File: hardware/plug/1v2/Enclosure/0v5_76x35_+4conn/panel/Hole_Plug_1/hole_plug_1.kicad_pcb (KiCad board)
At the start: 2 copper layers, 13.9 x 3.8 mm, 3 parts

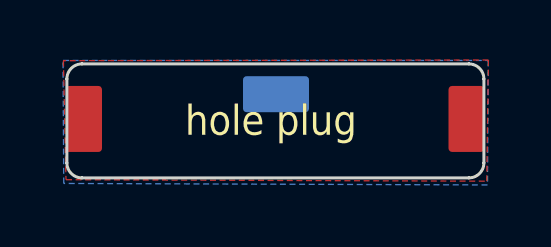
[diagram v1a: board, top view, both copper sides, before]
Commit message: add 3d models in .wrl
used @2ftg .step models and imported them into FreeCAD
added .wrl for Rear panels and hole plugs
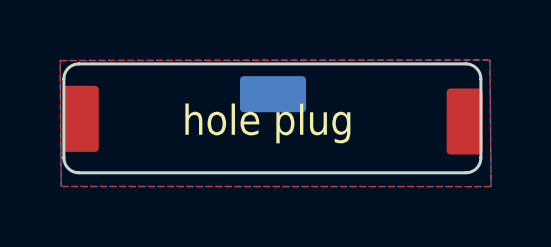
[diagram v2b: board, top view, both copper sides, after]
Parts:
- moved REF** 0.11 mm to (57.1, 117.4)
- moved REF** 0.10 mm to (69.9, 117.5)
- moved REF** 0.10 mm to (63.5, 116.6)
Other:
- board size 13.9 x 3.8 mm -> 13.9 x 3.6 mm
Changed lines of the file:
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@@
     (links 2)
     (no_connects 1)
-    (area 52.800953 112.2525 74.339048 124.249079)
+    (area 56.474999 115.499999 70.475001 119.230001)
     (thickness 1.6)
     (drawings 29)
@@
     (pad_to_mask_clearance 0)
     (aux_axis_origin 56.42 115.36)
-    (grid_origin 56.42 115.36)
+    (grid_origin 57.125 115.55)
     (visible_elements 7FFFFFFF)
     (pcbplotparams
@@
   )
   (module Connect:1pin (layer B.Cu)
-    (at 63.595 116.56 270)
+    (at 63.495 116.56 270)
     (descr "module 1 pin (ou trou mecanique de percage)")
     (tags DEV)
@@
   )
   (module Connect:1pin (layer F.Cu)
-    (at 57.195 117.385)
+    (at 57.085 117.38)
     (descr "module 1 pin (ou trou mecanique de percage)")
     (tags DEV)
@@
   )
   (module Connect:1pin (layer F.Cu)
-    (at 69.945 117.385)
+    (at 69.885 117.47)
     (descr "module 1 pin (ou trou mecanique de percage)")
     (tags DEV)
@@
       (net 1 GND) (zone_connect 1) (thermal_width 0.5) (thermal_gap 0.3))
   )
-  (gr_text "hole plug" (at 63.425 117.45) (layer F.SilkS)
+  (gr_text "hole plug" (at 63.325 117.45) (layer F.SilkS)
     (effects (font (size 1 0.9) (thickness 0.2)))
   )
-  (gr_line (start 57.125 119.35) (end 70.025 119.35) (layer Edge.Cuts) (width 0.1))
-  (gr_line (start 56.625 116.05) (end 56.625 118.85) (layer Edge.Cuts) (width 0.1))
-  (gr_line (start 70.025 115.55) (end 57.125 115.55) (layer Edge.Cuts) (width 0.1))
-  (gr_line (start 70.525 118.85) (end 70.525 116.05) (layer Edge.Cuts) (width 0.1))
-  (gr_arc (start 70.025 118.85) (end 70.525 118.85) (angle 90) (layer Edge.Cuts) (width 0.1))
-  (gr_arc (start 70.025 116.05) (end 70.025 115.55) (angle 90) (layer Edge.Cuts) (width 0.1))
-  (gr_arc (start 57.125 116.05) (end 56.625 116.05) (angle 90) (layer Edge.Cuts) (width 0.1))
-  (gr_arc (start 57.125 118.85) (end 57.125 119.35) (angle 90) (layer Edge.Cuts) (width 0.1))
+  (gr_line (start 57.025 119.18) (end 69.925 119.18) (layer Edge.Cuts) (width 0.1))
+  (gr_line (start 56.525 116.05) (end 56.525 118.68) (layer Edge.Cuts) (width 0.1))
+  (gr_line (start 69.925 115.55) (end 57.025 115.55) (layer Edge.Cuts) (width 0.1))
+  (gr_line (start 70.425 118.68) (end 70.425 116.05) (layer Edge.Cuts) (width 0.1))
+  (gr_arc (start 69.925 118.68) (end 70.425 118.68) (angle 90) (layer Edge.Cuts) (width 0.1))
+  (gr_arc (start 69.925 116.05) (end 69.925 115.55) (angle 90) (layer Edge.Cuts) (width 0.1))
+  (gr_arc (start 57.025 116.05) (end 56.525 116.05) (angle 90) (layer Edge.Cuts) (width 0.1))
+  (gr_arc (start 57.025 118.68) (end 57.025 119.18) (angle 90) (layer Edge.Cuts) (width 0.1))
   (gr_line (start 69.913521 119.199078) (end 57.413521 119.199078) (layer Dwgs.User) (width 0.1))
   (gr_line (start 57.413521 119.199078) (end 57.413521 124.199078) (layer Dwgs.User) (width 0.1))
@@
     (polygon
       (pts
-        (xy 56.595 119.41) (xy 70.62 119.46) (xy 70.675 115.42) (xy 56.508218 115.44276)
+        (xy 56.435 119.63) (xy 70.765 119.64) (xy 70.73 115.42) (xy 56.408218 115.44276)
       )
     )
@@
     (polygon
       (pts
-        (xy 56.495 115.435) (xy 70.67 115.435) (xy 70.645 119.585) (xy 56.52 119.535)
+        (xy 56.395 115.435) (xy 70.725 115.42) (xy 70.765 119.64) (xy 56.435 119.64)
       )
     )
